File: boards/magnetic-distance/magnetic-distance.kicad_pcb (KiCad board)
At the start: 2 copper layers, 25.5 x 15 mm, 8 parts, among them J101 Cable, U101 AS5304

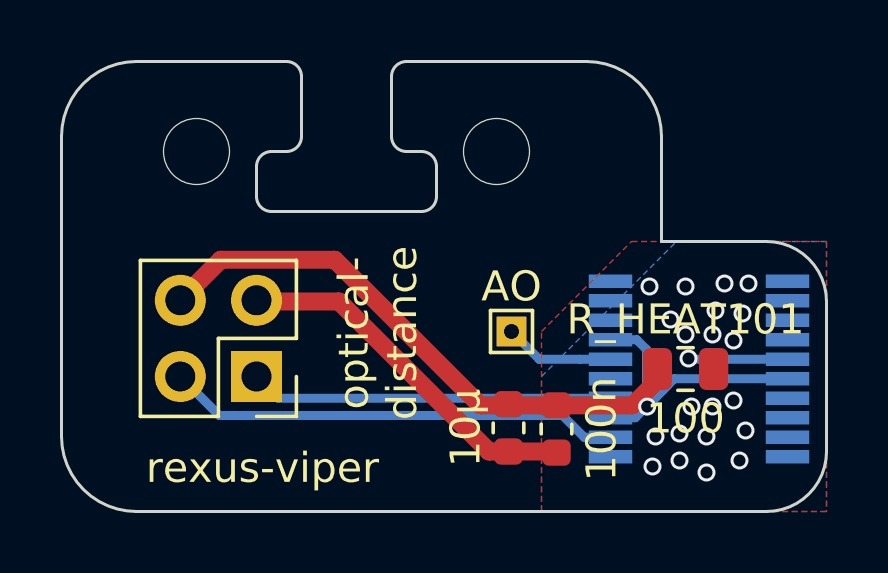
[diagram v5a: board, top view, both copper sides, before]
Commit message: [board][magnetic-distance] Place sensor chip correctly (on PCB front side)
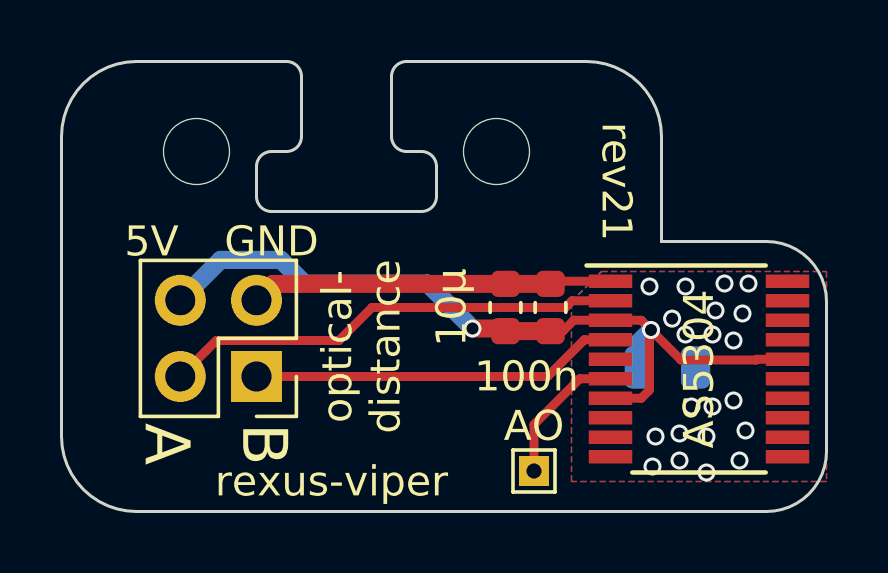
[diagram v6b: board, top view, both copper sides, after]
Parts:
- R_HEAT101: moved to B.Cu
- U101: moved to F.Cu
- moved TP101 4.71 mm to (100.8, 47.6)
- moved C101 4.05 mm to (101.3, 42.2), turned to 90 degrees
- moved C102 4.01 mm to (99.8, 42.2), turned to 90 degrees
- moved R_HEAT101 0.60 mm to (105.2, 44.2)
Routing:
- net +5V: track 31.9 -> 27.4 mm, vias 1 -> 2
- net GND: track 15.6 -> 12.1 mm, vias 22 -> 21
- net /AO: track 3.68 -> 4.73 mm
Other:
- board text added: "AO"
- board text added: "rev21"
- board text removed: "rev20"
